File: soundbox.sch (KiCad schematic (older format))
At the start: 165 parts, among them J10 COLOR INPUT, J11 MONO INPUT, J12 NEXT PWR INPUT 1, J13 NEXT PWR INPUT 2, J14 -12VDC OUT, J15 5VDC STANDBY, J16 MON IN 1, J17 MON IN 2, J18 PA1, J19 BOOT0, J2 OUT (SJ1-3535NG), J20 PC0, J21 PC1, J22 PB0, J23 PB1, J24 R SPK, J25 R SPEAKER (SJ-2509N), J26 L SPEAKER, J27 L SPK, J3 MIC (SJ1-3535NG), J31 NeXT Keyboard, J32 NeXT Keyboard (MD-50SM / KMDG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, J4 USB Host (SS-52100-001), J5 Mic IN, J6 Audio OUT, J7 STLINK, J8 UART2, J9 PA0, Q1 2SC2712, SW1 NeXT POWER SW (1-1825027-1 / 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, SW3 NeXT POWER SW, SW4 RESET, U11 TLV70033DDCR, U17 USBLC6-2SC6, U18 STMPS2141STR, U19 SN74LVC2G34DBV, U20 PCM5122PW, U21 TLV70033DDCR, U22 TLV70033DDCR, U23 PLT133/T, U24 STM32F401RCT6, U25 SN74LVC1G07DBV, U26 SN74HCT125DR, U27 TLV320ADC3100, U28 BD33FC0FP, U29 TPA2005D1DGN, U30 BD33FC0FP, U31 TPA2005D1DGN, U8 5V(DC/DC), X3 ECS-2520MVLC-225.792-BN-TR, Y2 25MHz (FA-238 25.0000MB-K0)

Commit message: add more tracks
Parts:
- added C172: 0.1u, Capacitor_SMD:C_0603_1608Metric_Pad1.05x0.95mm_HandSolder, symbol Device:C
- added NT1: AGND_DGND, NetTie:NetTie-2_SMD_Pad0.5mm, symbol Device:Net-Tie_2
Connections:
- net GND: now also C172.2, NT1.2; no longer C102.2, C111.2, C114.2, C118.2, C121.1, C122.1, C123.2, C135.1, C136.1, C140.2, C141.1, C142.2, C143.2, C146.1, C147.1, C148.2, C151.2, C152.2, C153.2, C154.1, C155.1, C157.2, C159.1, C160.1, C161.2, C164.2, C165.2, C166.2, C167.1, C168.1, C170.2, J2.S, J3.S, J5.1 (Pin_1), J6.1 (Pin_1), U20.3 (CPGND), U20.9 (AGND), U22.2 (GND), U27.9 (AVSS), U28.2 (GND), U29.7 (GND), U29.9 (Therm), U30.2 (GND), U31.7 (GND), U31.9 (Therm)
- net at C107.1, C126.1, C36.1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: now also C172.1
- new net GNDA: C102.2, C111.2, C114.2, C118.2, C121.1, C122.1, C123.2, C135.1, C136.1, C140.2, C141.1, C142.2, C143.2, C146.1, C147.1, C148.2, C151.2, C152.2, C153.2, C154.1, C155.1, C157.2, C159.1, C160.1, C161.2, C164.2, C165.2, C166.2, C167.1, C168.1, C170.2, J2.S, J3.S, J5.1 (Pin_1), J6.1 (Pin_1), NT1.1, U20.3 (CPGND), U20.9 (AGND), U22.2 (GND), U27.9 (AVSS), U28.2 (GND), U29.7 (GND), U29.9 (Therm), U30.2 (GND), U31.7 (GND), U31.9 (Therm)
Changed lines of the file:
@@
 L ossc_board-rescue:GND-RESCUE-ossc_board #PWR0233
 U 1 1 5F942C4C
-P 14400 2500
-F 0 "#PWR0233" H 14400 2500 30  0001 C CNN
-F 1 "GND-RESCUE-ossc_board" H 14400 2430 30  0001 C CNN
-F 2 "" H 14400 2500 60  0000 C CNN
-F 3 "" H 14400 2500 60  0000 C CNN
-	1    14400 2500
+P 14450 2500
+F 0 "#PWR0233" H 14450 2500 30  0001 C CNN
+F 1 "GND-RESCUE-ossc_board" H 14450 2430 30  0001 C CNN
+F 2 "" H 14450 2500 60  0000 C CNN
+F 3 "" H 14450 2500 60  0000 C CNN
+	1    14450 2500
 	1    0    0    -1
 $EndComp
@@
 	14250 2450 14250 2400
 Wire Wire Line
-	14250 2400 14400 2400
-Wire Wire Line
-	14400 2400 14400 2500
-Wire Wire Line
 	12850 3350 12850 3450
 $Comp
@@
 Wire Wire Line
 	15250 9450 15350 9450
+$Comp
+L Device:C C172
+U 1 1 5F4F54DB
+P 8800 4150
+F 0 "C172" H 8915 4196 50  0000 L CNN
+F 1 "0.1u" H 8915 4105 50  0000 L CNN
+F 2 "Capacitor_SMD:C_0603_1608Metric_Pad1.05x0.95mm_HandSolder" H 8838 4000 50  0001 C CNN
+F 3 "~" H 8800 4150 50  0001 C CNN
+	1    8800 4150
+	1    0    0    -1
+$EndComp
+Wire Wire Line
+	9100 3900 8800 3900
+Connection ~ 9100 3900
+Wire Wire Line
+	8800 3900 8800 4000
+Wire Wire Line
+	9100 4300 8800 4300
+Connection ~ 9100 4300
+$Comp
+L Device:Net-Tie_2 NT1
+U 1 1 5FA7FE16
+P 14350 2400
+F 0 "NT1" H 14350 2581 50  0000 C CNN
+F 1 "AGND_DGND" H 14350 2490 50  0000 C CNN
+F 2 "NetTie:NetTie-2_SMD_Pad0.5mm" H 14350 2400 50  0001 C CNN
+F 3 "~" H 14350 2400 50  0001 C CNN
+	1    14350 2400
+	1    0    0    -1
+$EndComp
+Wire Wire Line
+	14450 2400 14450 2500
 $EndSCHEMATC

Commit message: update ground
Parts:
- NT1: footprint NetTie:NetTie-2_SMD_Pad0.5mm -> NetTie:NetTie-2_SMD_Pad2.0mm
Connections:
- net GND: no longer C112.1, C113.2
- net GNDA: now also C112.1, C113.2
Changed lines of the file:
@@
 	0    1    1    0
 $EndComp
-$Comp
-L ossc_board-rescue:GND-RESCUE-ossc_board #PWR0230
-U 1 1 5F8D70CF
-P 13250 2150
-F 0 "#PWR0230" H 13250 2150 30  0001 C CNN
-F 1 "GND-RESCUE-ossc_board" H 13250 2080 30  0001 C CNN
-F 2 "" H 13250 2150 60  0000 C CNN
-F 3 "" H 13250 2150 60  0000 C CNN
-	1    13250 2150
-	1    0    0    -1
-$EndComp
-$Comp
-L ossc_board-rescue:GND-RESCUE-ossc_board #PWR0231
-U 1 1 5F8D7698
-P 13250 1250
-F 0 "#PWR0231" H 13250 1250 30  0001 C CNN
-F 1 "GND-RESCUE-ossc_board" H 13250 1180 30  0001 C CNN
-F 2 "" H 13250 1250 60  0000 C CNN
-F 3 "" H 13250 1250 60  0000 C CNN
-	1    13250 1250
-	-1   0    0    1
-$EndComp
 Wire Wire Line
 	13150 1650 13250 1650
@@
 Wire Wire Line
 	12750 1650 12850 1650
-Wire Wire Line
-	13250 1350 13250 1250
-Wire Wire Line
-	13250 2050 13250 2150
 NoConn ~ 12750 1950
 NoConn ~ 12750 2050
@@
 F 0 "NT1" H 14350 2581 50  0000 C CNN
 F 1 "AGND_DGND" H 14350 2490 50  0000 C CNN
-F 2 "NetTie:NetTie-2_SMD_Pad0.5mm" H 14350 2400 50  0001 C CNN
+F 2 "NetTie:NetTie-2_SMD_Pad2.0mm" H 14350 2400 50  0001 C CNN
 F 3 "~" H 14350 2400 50  0001 C CNN
 	1    14350 2400
@@
 Wire Wire Line
 	14450 2400 14450 2500
+$Comp
+L power:GNDA #PWR?
+U 1 1 5F63E69C
+P 13250 2050
+F 0 "#PWR?" H 13250 1800 50  0001 C CNN
+F 1 "GNDA" H 13255 1877 50  0000 C CNN
+F 2 "" H 13250 2050 50  0001 C CNN
+F 3 "" H 13250 2050 50  0001 C CNN
+	1    13250 2050
+	1    0    0    -1
+$EndComp
+$Comp
+L power:GNDA #PWR?
+U 1 1 5F7AFB76
+P 13250 1350
+F 0 "#PWR?" H 13250 1100 50  0001 C CNN
+F 1 "GNDA" H 13255 1177 50  0000 C CNN
+F 2 "" H 13250 1350 50  0001 C CNN
+F 3 "" H 13250 1350 50  0001 C CNN
+	1    13250 1350
+	-1   0    0    1
+$EndComp
 $EndSCHEMATC

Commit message: finish tracks
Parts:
- U29, U31: footprint Package_SO:MSOP-8-1EP_3x3mm_P0.65mm_EP1.73x1.85mm_ThermalVias -> Package_SO:MSOP-8-1EP_3x3mm_P0.65mm_EP1.73x1.85mm
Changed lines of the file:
@@
 F 0 "U31" H 13200 11137 60  0000 C CNN
 F 1 "TPA2005D1DGN" H 13200 11031 60  0000 C CNN
-F 2 "Package_SO:MSOP-8-1EP_3x3mm_P0.65mm_EP1.73x1.85mm_ThermalVias" H 12600 9650 60  0001 C CNN
+F 2 "Package_SO:MSOP-8-1EP_3x3mm_P0.65mm_EP1.73x1.85mm" H 12600 9650 60  0001 C CNN
 F 3 "" H 12600 9650 60  0001 C CNN
 	1    13250 10050
@@
 F 0 "U29" H 13500 6087 60  0000 C CNN
 F 1 "TPA2005D1DGN" H 13500 5981 60  0000 C CNN
-F 2 "Package_SO:MSOP-8-1EP_3x3mm_P0.65mm_EP1.73x1.85mm_ThermalVias" H 12900 4600 60  0001 C CNN
+F 2 "Package_SO:MSOP-8-1EP_3x3mm_P0.65mm_EP1.73x1.85mm" H 12900 4600 60  0001 C CNN
 F 3 "" H 12900 4600 60  0001 C CNN
 	1    13550 5000
@@
 	14450 2400 14450 2500
 $Comp
-L power:GNDA #PWR?
+L power:GNDA #PWR0230
 U 1 1 5F63E69C
 P 13250 2050
-F 0 "#PWR?" H 13250 1800 50  0001 C CNN
+F 0 "#PWR0230" H 13250 1800 50  0001 C CNN
 F 1 "GNDA" H 13255 1877 50  0000 C CNN
 F 2 "" H 13250 2050 50  0001 C CNN
@@
 $EndComp
 $Comp
-L power:GNDA #PWR?
+L power:GNDA #PWR0231
 U 1 1 5F7AFB76
 P 13250 1350
-F 0 "#PWR?" H 13250 1100 50  0001 C CNN
+F 0 "#PWR0231" H 13250 1100 50  0001 C CNN
 F 1 "GNDA" H 13255 1177 50  0000 C CNN
 F 2 "" H 13250 1350 50  0001 C CNN

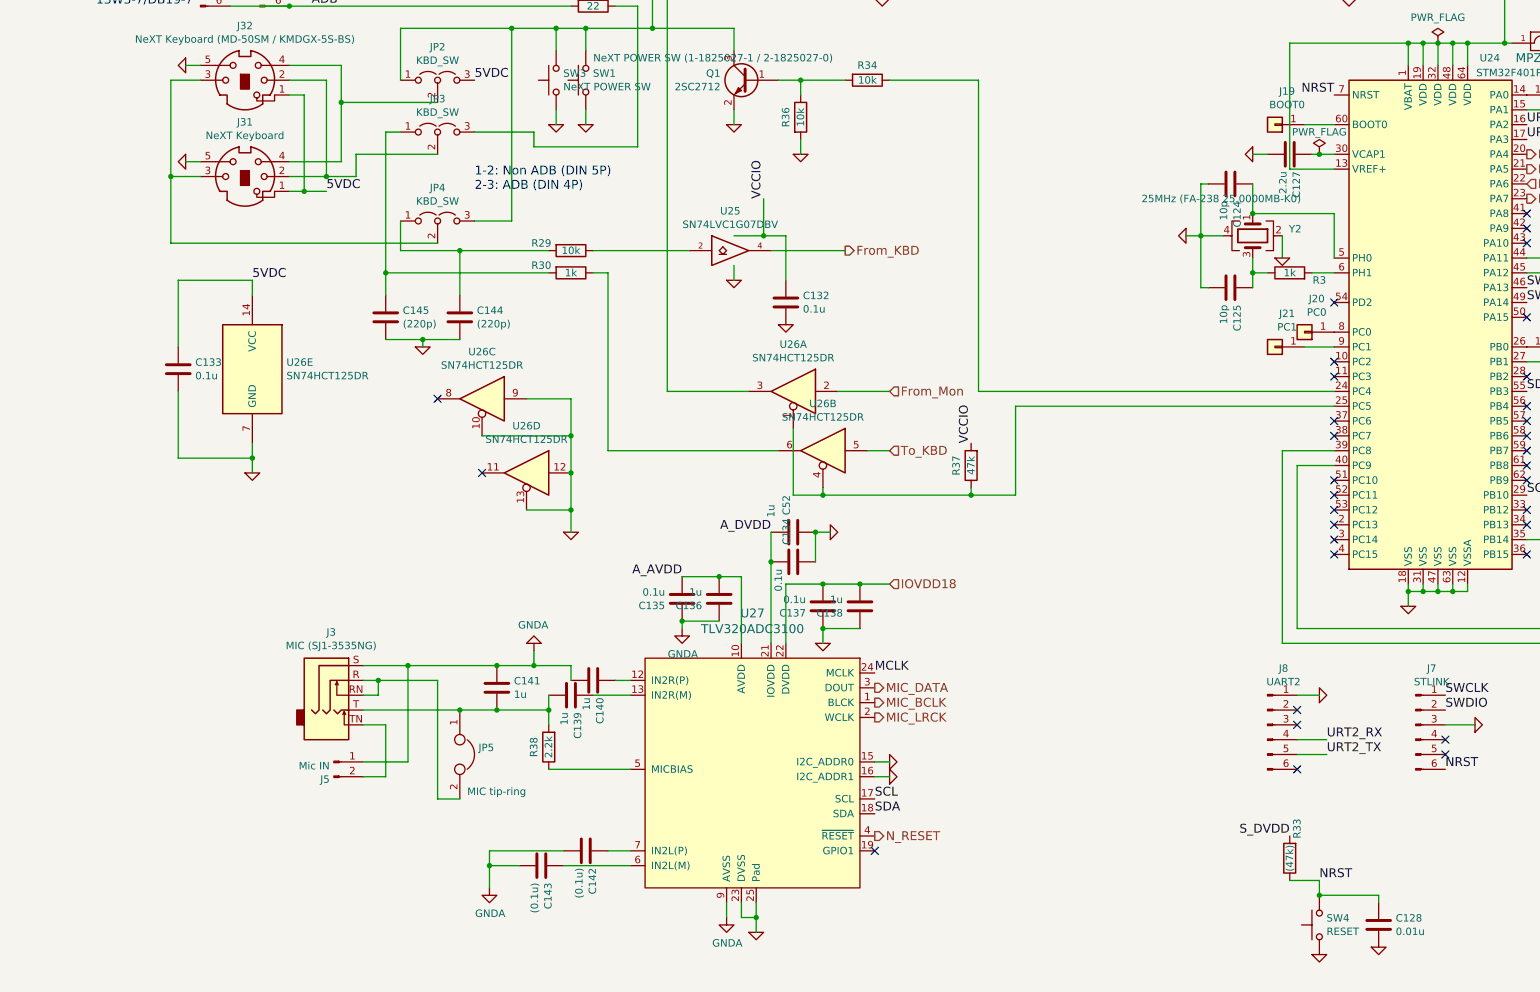
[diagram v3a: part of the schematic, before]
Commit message: add optional components
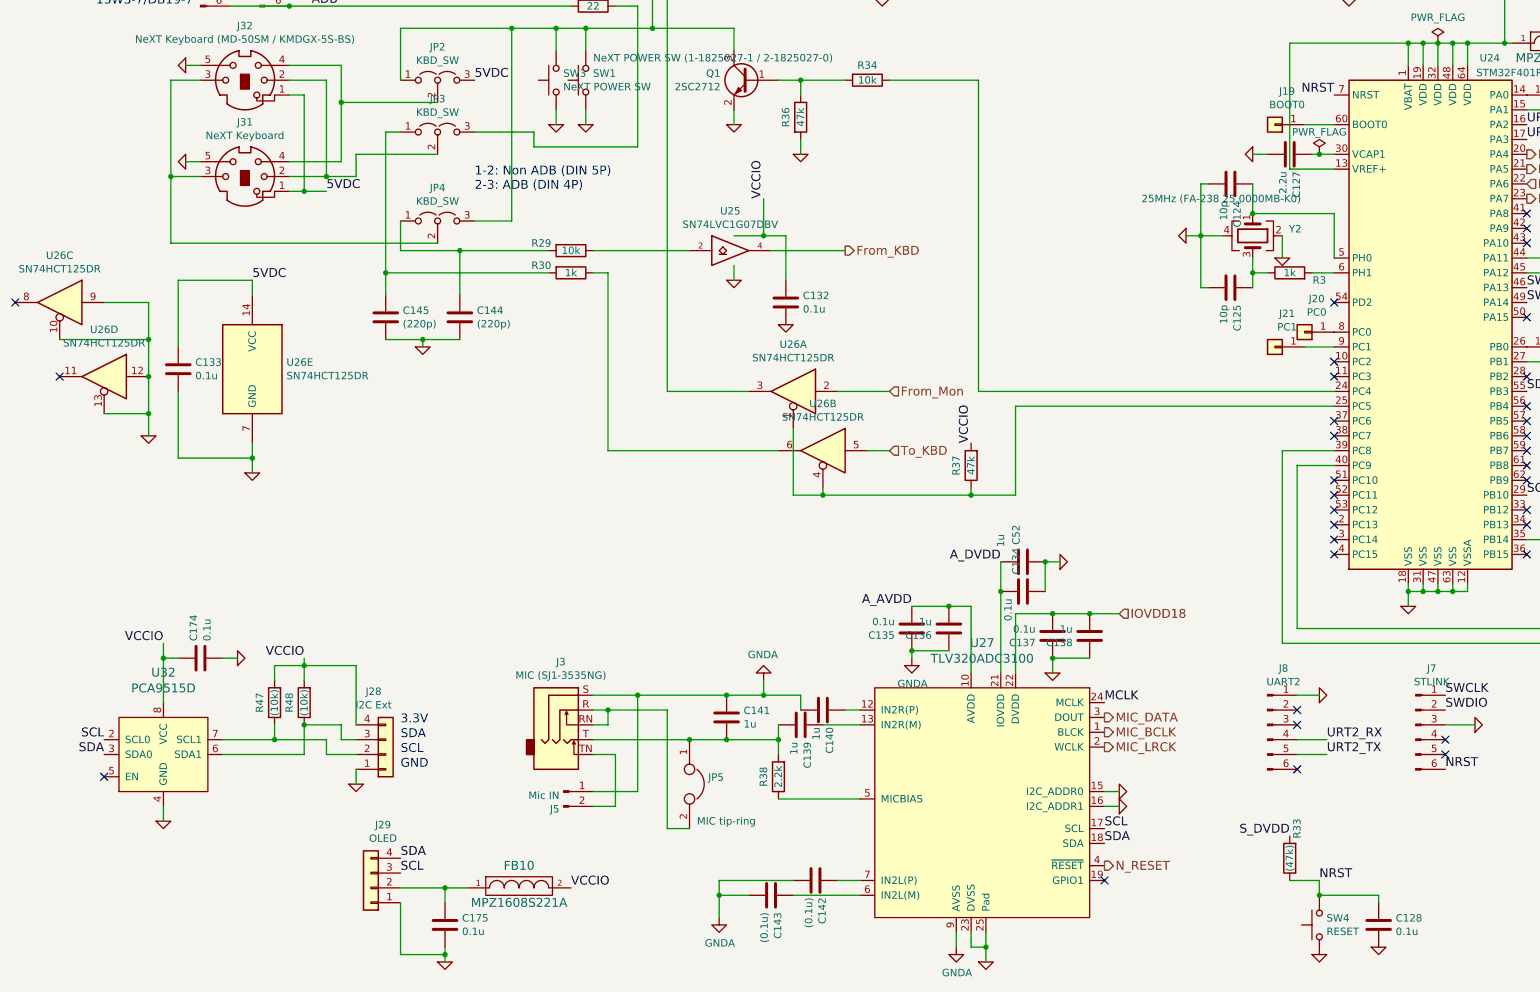
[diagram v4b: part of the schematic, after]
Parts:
- added C174, C175: 0.1u, Capacitor_SMD:C_0603_1608Metric_Pad1.05x0.95mm_HandSolder, symbol Device:C
- added FB10: MPZ1608S221A, Inductor_SMD:L_0603_1608Metric_Pad1.05x0.95mm_HandSolder, symbol ossc_board-rescue:FILTER
- added J28: I2C Ext, Connector_JST:JST_XH_B4B-XH-A_1x04_P2.50mm_Vertical, symbol Connector_Generic:Conn_01x04
- added J29: OLED, custom_components:OLED_0.91inch_I2C, symbol Connector_Generic:Conn_01x04
- added R47, R48: (10k), Resistor_SMD:R_0603_1608Metric_Pad1.05x0.95mm_HandSolder, symbol Device:R
- added U32: PCA9515D, Package_SO:SOIC-8_3.9x4.9mm_P1.27mm, symbol custom_components:PCA9515
- C128: value 0.01u -> 0.1u
- R36: value 10k -> 47k
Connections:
- net GND: now also C174.2, C175.2, J28.1 (Pin_1), J29.1 (Pin_1), U32.4 (GND)
- net SCL: now also J29.3 (Pin_3), U32.2 (SCL0)
- net SDA: now also J29.4 (Pin_4), U32.3 (SDA0)
- net VCC: now also C174.1, FB10.2, J28.4 (Pin_4), R47.2, R48.2, U32.8 (VCC)
- new net: J28.3 (Pin_3), R48.1, U32.6 (SDA1)
- new net: J28.2 (Pin_2), R47.1, U32.7 (SCL1)
- new net: C175.1, FB10.1, J29.2 (Pin_2)
- no-connect marks 40 -> 41
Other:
- note added: "3.3V"
- note added: "GND"
- note added: "SCL"
- note added: "SDA"
- moved on the sheet: C134, C135, C136, C137, C138, C139, C140, C141, C142, C143, C52, J3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

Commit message: minor update
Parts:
- R31: value 120 5W -> 2x 120 5W (or 56ohm 7W)
- R34: value 10k -> 4.7k
- SW4: value RESET -> MCU RESET
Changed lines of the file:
@@
 EESchema Schematic File Version 4
-LIBS:ossc_board-cache
 EELAYER 30 0
 EELAYER END
@@
 P 2700 2250
 F 0 "R31" H 2770 2296 50  0000 L CNN
-F 1 "120 5W" H 2770 2205 50  0000 L CNN
+F 1 "2x 120 5W (or 56ohm 7W)" H 2770 2205 50  0000 L CNN
 F 2 "Resistor_THT:R_Axial_DIN0617_L17.0mm_D6.0mm_P30.48mm_Horizontal" V 2630 2250 50  0001 C CNN
 F 3 "~" H 2700 2250 50  0001 C CNN
@@
 P 9150 10650
 F 0 "SW4" V 9196 10602 50  0000 R CNN
-F 1 "RESET" V 9105 10602 50  0000 R CNN
+F 1 "MCU RESET" V 8850 10750 50  0000 R CNN
 F 2 "Button_Switch_THT:SW_PUSH_6mm" H 9150 10850 50  0001 C CNN
 F 3 "~" H 9150 10850 50  0001 C CNN
@@
 P 6100 4950
 F 0 "R34" V 6000 4950 50  0000 C CNN
-F 1 "10k" V 6100 4950 50  0000 C CNN
+F 1 "4.7k" V 6100 4950 50  0000 C CNN
 F 2 "Resistor_SMD:R_0603_1608Metric_Pad1.05x0.95mm_HandSolder" V 6030 4950 50  0001 C CNN
 F 3 "~" H 6100 4950 50  0001 C CNN

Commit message: update values
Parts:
- added R49: 22-150, Resistor_SMD:R_0603_1608Metric_Pad1.05x0.95mm_HandSolder, symbol Device:R
- C112: value 2200p -> 2200p (GRM1885C1H222JA01J)
- C115: value 2.2u -> 2.2u (GRM188R71A225KE15D)
- C3: value 1u -> 1u (GRT188R61H105KE13D)
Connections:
- net GREEN_OUT: now also R49.2; no longer J11.2 (Pin_2)
- new net MONO_VIDEO: J11.2 (Pin_2), R49.1
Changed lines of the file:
@@
 BLUE_OUT
 Wire Wire Line
-	1600 1100 1500 1100
-Wire Wire Line
-	1600 1100 2200 1100
-Connection ~ 1600 1100
+	1600 1100 1550 1100
 Wire Wire Line
 	2300 1200 2200 1200
@@
 P 3450 3250
 F 0 "C3" H 3565 3296 50  0000 L CNN
-F 1 "1u" H 3565 3205 50  0000 L CNN
+F 1 "1u (GRT188R61H105KE13D)" H 3565 3205 50  0000 L CNN
 F 2 "Capacitor_SMD:C_0603_1608Metric_Pad1.05x0.95mm_HandSolder" H 3488 3100 50  0001 C CNN
 F 3 "~" H 3450 3250 50  0001 C CNN
@@
 P 13250 1500
 F 0 "C112" H 13365 1546 50  0000 L CNN
-F 1 "2200p" H 13365 1455 50  0000 L CNN
+F 1 "2200p (GRM1885C1H222JA01J)" H 12950 1650 50  0000 L CNN
 F 2 "Capacitor_SMD:C_0603_1608Metric_Pad1.05x0.95mm_HandSolder" H 13288 1350 50  0001 C CNN
 F 3 "~" H 13250 1500 50  0001 C CNN
@@
 U 1 1 5F958F84
 P 13050 2750
-F 0 "C115" H 13165 2796 50  0000 L CNN
-F 1 "2.2u" H 13165 2705 50  0000 L CNN
+F 0 "C115" V 13100 2350 50  0000 L CNN
+F 1 "2.2u (GRM188R71A225KE15D)" V 13000 1400 50  0000 L CNN
 F 2 "Capacitor_SMD:C_0603_1608Metric_Pad1.05x0.95mm_HandSolder" H 13088 2600 50  0001 C CNN
 F 3 "~" H 13050 2750 50  0001 C CNN
@@
 MONO_VIDEO
 Wire Wire Line
-	2300 1100 2200 1100
-Connection ~ 2200 1100
+	2300 1100 2250 1100
 $Comp
 L power:PWR_FLAG #FLG0101
@@
 Text Label 2950 10200 0    60   ~ 0
 SDA
+$Comp
+L Device:R R49
+U 1 1 5F6182A3
+P 1900 650
+F 0 "R49" V 1800 650 50  0000 C CNN
+F 1 "22-150" V 1900 650 50  0000 C CNN
+F 2 "Resistor_SMD:R_0603_1608Metric_Pad1.05x0.95mm_HandSolder" V 1830 650 50  0001 C CNN
+F 3 "~" H 1900 650 50  0001 C CNN
+	1    1900 650
+	0    1    1    0
+$EndComp
+Wire Wire Line
+	2250 1100 2250 650
+Wire Wire Line
+	2250 650  2050 650
+Connection ~ 2250 1100
+Wire Wire Line
+	2250 1100 2200 1100
+Wire Wire Line
+	1550 1100 1550 650
+Wire Wire Line
+	1550 650  1750 650
+Connection ~ 1550 1100
+Wire Wire Line
+	1550 1100 1500 1100
 $EndSCHEMATC

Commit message: update
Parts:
- added R13, R14: 2.2k, Resistor_SMD:R_0603_1608Metric_Pad1.05x0.95mm_HandSolder, symbol Device:R
- added R50: 10k, Resistor_SMD:R_0603_1608Metric_Pad1.05x0.95mm_HandSolder, symbol Device:R
- C142, C143: value (0.1u) -> 0.1u
- R47, R48: value (10k) -> 10k
- U21, U22: value TLV70033DDCR -> TLV70033DDCR (or XC6204B332MR-G)
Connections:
- net GND: now also U17.2 (GND)
- net SCL: now also R14.2
- net SDA: now also R13.2
- net S_DVDD: now also R13.1, R14.1
- net VCC: now also R50.1
- net at J4.1 (VBUS), U18.1 (OUT): now also U17.5 (VBUS)
- net at U24.44 (PA11): now also U17.3 (I/O2)
- net at U24.45 (PA12): now also U17.1 (I/O1)
- net at U24.53 (PC12): now also R50.2
- net at J4.2 (D-): now also U17.4 (I/O2)
- net at J4.3 (D+): now also U17.6 (I/O1)
- no-connect marks 41 -> 40
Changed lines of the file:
@@
 P 6700 1150
 F 0 "U21" H 6700 1492 50  0000 C CNN
-F 1 "TLV70033DDCR" H 6700 1401 50  0000 C CNN
+F 1 "TLV70033DDCR (or XC6204B332MR-G)" H 6700 1401 50  0000 C CNN
 F 2 "custom_components:SOT-23-5_Handsoldering" H 6700 1450 50  0001 C CIN
 F 3 "http://www.ti.com/lit/ds/symlink/tlv712.pdf" H 6700 1150 50  0001 C CNN
@@
 P 8450 1150
 F 0 "U22" H 8450 1492 50  0000 C CNN
-F 1 "TLV70033DDCR" H 8450 1401 50  0000 C CNN
+F 1 "TLV70033DDCR (or XC6204B332MR-G)" H 8450 1401 50  0000 C CNN
 F 2 "custom_components:SOT-23-5_Handsoldering" H 8450 1450 50  0001 C CIN
 F 3 "http://www.ti.com/lit/ds/symlink/tlv712.pdf" H 8450 1150 50  0001 C CNN
@@
 SDA
 Wire Wire Line
-	11350 2150 10350 2150
-Wire Wire Line
-	10350 2250 11350 2250
+	11350 2150 10650 2150
 Text HLabel 10700 1650 0    60   Output ~ 0
 Audio_MCK
@@
 NoConn ~ 9250 8050
 NoConn ~ 9250 7950
-NoConn ~ 9250 7850
 NoConn ~ 9250 7750
 NoConn ~ 9250 7650
@@
 P 5450 10450
 F 0 "C143" H 5565 10496 50  0000 L CNN
-F 1 "(0.1u)" H 5565 10405 50  0000 L CNN
+F 1 "0.1u" H 5565 10405 50  0000 L CNN
 F 2 "Capacitor_SMD:C_0603_1608Metric_Pad1.05x0.95mm_HandSolder" H 5488 10300 50  0001 C CNN
 F 3 "~" H 5450 10450 50  0001 C CNN
@@
 P 5750 10350
 F 0 "C142" H 5865 10396 50  0000 L CNN
-F 1 "(0.1u)" H 5865 10305 50  0000 L CNN
+F 1 "0.1u" H 5865 10305 50  0000 L CNN
 F 2 "Capacitor_SMD:C_0603_1608Metric_Pad1.05x0.95mm_HandSolder" H 5788 10200 50  0001 C CNN
 F 3 "~" H 5750 10350 50  0001 C CNN
@@
 P 2100 9150
 F 0 "R47" V 2200 9150 50  0000 C CNN
-F 1 "(10k)" V 2100 9150 50  0000 C CNN
+F 1 "10k" V 2100 9150 50  0000 C CNN
 F 2 "Resistor_SMD:R_0603_1608Metric_Pad1.05x0.95mm_HandSolder" V 2030 9150 50  0001 C CNN
 F 3 "~" H 2100 9150 50  0001 C CNN
@@
 P 2300 9150
 F 0 "R48" V 2400 9150 50  0000 C CNN
-F 1 "(10k)" V 2300 9150 50  0000 C CNN
+F 1 "10k" V 2300 9150 50  0000 C CNN
 F 2 "Resistor_SMD:R_0603_1608Metric_Pad1.05x0.95mm_HandSolder" V 2230 9150 50  0001 C CNN
 F 3 "~" H 2300 9150 50  0001 C CNN
@@
 Wire Wire Line
 	1550 1100 1500 1100
+$Comp
+L Device:R R13
+U 1 1 5F58C9D7
+P 10450 2700
+F 0 "R13" V 10550 2700 50  0000 C CNN
+F 1 "2.2k" V 10450 2700 50  0000 C CNN
+F 2 "Resistor_SMD:R_0603_1608Metric_Pad1.05x0.95mm_HandSolder" V 10380 2700 50  0001 C CNN
+F 3 "~" H 10450 2700 50  0001 C CNN
+	1    10450 2700
+	-1   0    0    1
+$EndComp
+$Comp
+L Device:R R14
+U 1 1 5F58E410
+P 10650 2700
+F 0 "R14" V 10750 2700 50  0000 C CNN
+F 1 "2.2k" V 10650 2700 50  0000 C CNN
+F 2 "Resistor_SMD:R_0603_1608Metric_Pad1.05x0.95mm_HandSolder" V 10580 2700 50  0001 C CNN
+F 3 "~" H 10650 2700 50  0001 C CNN
+	1    10650 2700
+	-1   0    0    1
+$EndComp
+Text Label 10650 3000 0    60   ~ 0
+S_DVDD
+Wire Wire Line
+	10650 2850 10650 3000
+Wire Wire Line
+	10650 2850 10450 2850
+Connection ~ 10650 2850
+Wire Wire Line
+	10450 2550 10450 2250
+Wire Wire Line
+	10350 2250 10450 2250
+Connection ~ 10450 2250
+Wire Wire Line
+	10450 2250 11350 2250
+Wire Wire Line
+	10650 2550 10650 2150
+Connection ~ 10650 2150
+Wire Wire Line
+	10650 2150 10350 2150
+Wire Wire Line
+	13700 7000 13700 7100
+Wire Wire Line
+	13900 7000 13900 7100
+Wire Wire Line
+	13300 7500 13400 7500
+Wire Wire Line
+	13700 8000 13700 7900
+Wire Wire Line
+	13900 7900 13900 8000
+Wire Wire Line
+	14300 7500 14200 7500
+$Comp
+L Device:R R50
+U 1 1 5FAA3175
+P 8600 7850
+F 0 "R50" V 8700 7850 50  0000 C CNN
+F 1 "10k" V 8600 7850 50  0000 C CNN
+F 2 "Resistor_SMD:R_0603_1608Metric_Pad1.05x0.95mm_HandSolder" V 8530 7850 50  0001 C CNN
+F 3 "~" H 8600 7850 50  0001 C CNN
+	1    8600 7850
+	0    -1   -1   0
+$EndComp
+Text Label 8450 7850 1    60   ~ 0
+VCCIO
+Wire Wire Line
+	9250 7850 8750 7850
 $EndSCHEMATC
